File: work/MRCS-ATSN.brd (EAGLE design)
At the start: 159.8 x 68.8 mm, 63 parts, among them IC1 LM324N, IC2 LM324N, J1 RJ14, J2 RJ14, Q1 2N4401, Q2 2N4403, T1 TY-145P

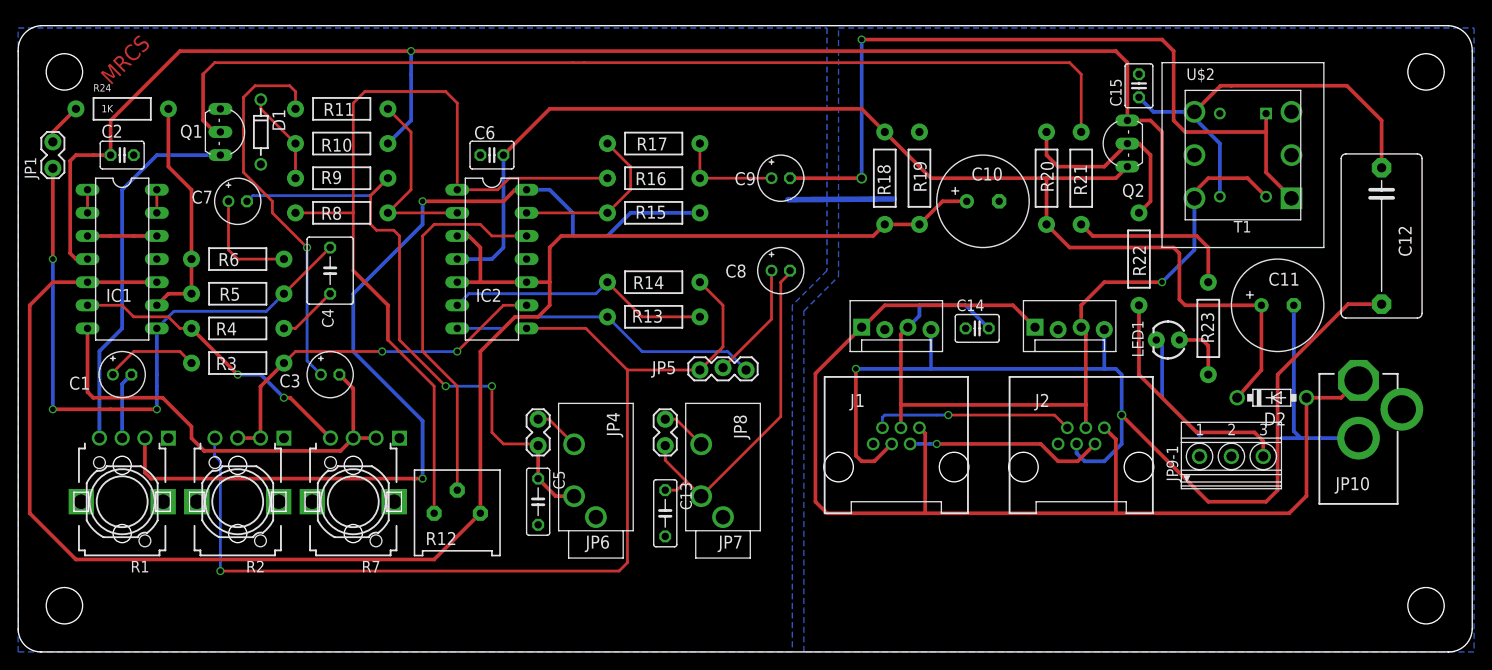
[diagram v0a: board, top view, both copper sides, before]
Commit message: clean up of messy import
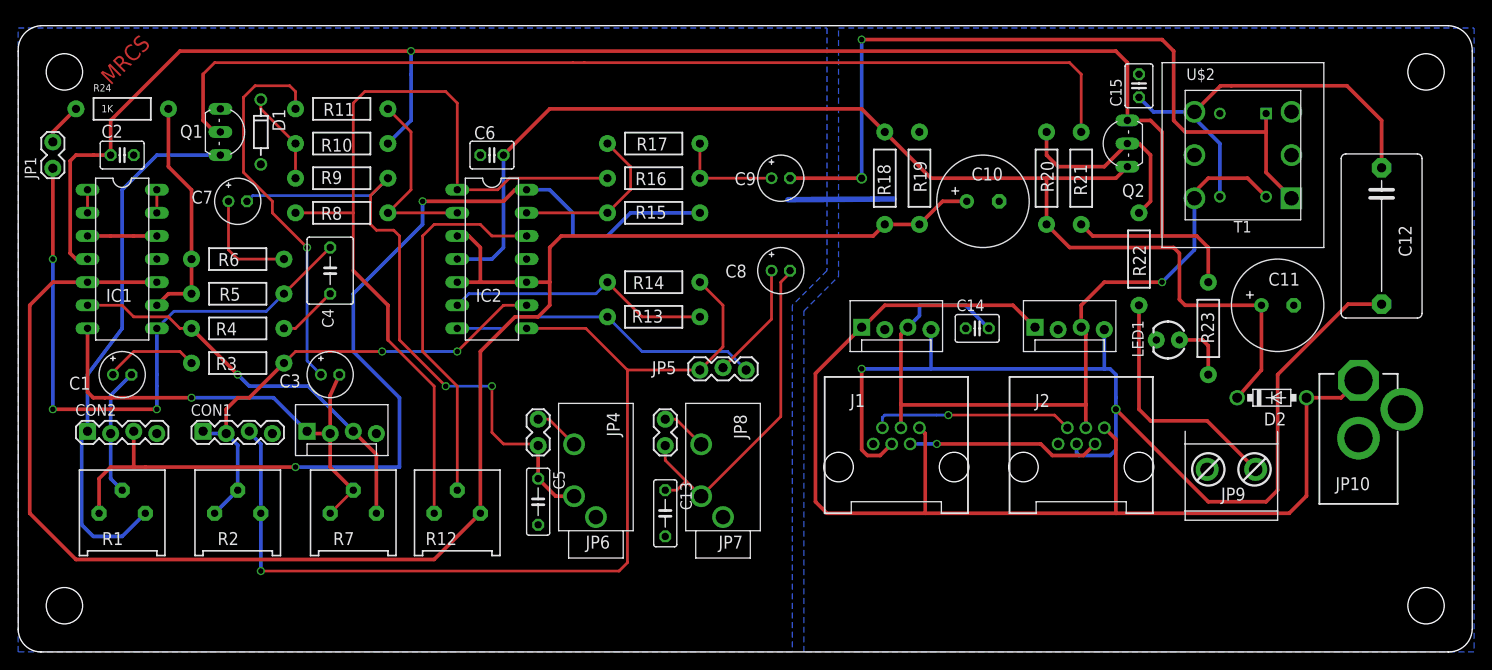
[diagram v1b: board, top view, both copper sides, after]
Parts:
- removed JP9-1: 1751251, con-phoenix-350:1751251
- added CON1: Audio, SPCoast 2017_04:1X04_LOCK
- added CON2: Break-In, SPCoast 2017_04:1X04_LOCK
- added JP9: (no value), SPCoast:MSTB2
- added SL3: (no value), SPCoast:MOLEX-1X4_LOCK
- C10, C11: device rcl:E3,5-10 -> rcl:E3.5-10
- POWER: device SPCoast:PWR_LABEL -> SPCoast:POWER_USAGE
- R1: value 10kA -> 10K; device SPCoast:R-POT-MRCS -> bourns_test:3386K
- R2: value 100kA -> 100K; device SPCoast:R-POT-MRCS -> bourns_test:3386K
- R7: value 500kA -> 500K; device SPCoast:R-POT-MRCS -> bourns_test:3386K
- moved R1 1.27 mm to (11.4, 15.2), turned to 0 degrees
- moved R2 1.27 mm to (24.1, 15.2), turned to 0 degrees
- moved R7 1.27 mm to (36.8, 15.2), turned to 0 degrees
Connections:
- removed net N$9: JP9-1.3, R22.P$1
- new net N$16: JP9.2, R22.P$1
- net GND: now also CON1.4, CON2.4, JP9.1, SL3.4; no longer JP9-1.1, JP9-1.2, R1.GND, R1.M1, R1.M2, R2.GND, R2.M1, R2.M2, R7.GND, R7.M1, R7.M2
- net N$13: now also SL3.1, SL3.2
- net N$20: now also CON1.1, CON1.2
- net N$38: now also SL3.3
- net N$40: now also CON1.3
- net RXGAIN: now also CON2.2
- net RXLEVEL: now also CON2.3
- net TXGND: now also CON2.1
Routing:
- net GND: track 47.5 -> 11.7 mm
- net N$16: track 0.00 -> 27.0 mm
- net N$9: track 26.0 -> 0.00 mm
- net TXGND: track 40.7 -> 59.3 mm
- net N$20: track 41.1 -> 53.5 mm
- net N$38: track 32.8 -> 45.0 mm, vias 2 -> 1
- net RXGAIN: track 7.39 -> 14.2 mm
- net RXLEVEL: track 107.0 -> 111.4 mm
- net N$40: track 113.9 -> 110.7 mm
- net N$13: track 50.3 -> 53.1 mm, vias 0 -> 1
- net RING: track 116.4 -> 113.7 mm
- net N$7: track 21.9 -> 21.4 mm
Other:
- board text added: "2017-08"
- board text added: "White soldermask / Black silkscreen"
- board text added: "rev 0.5"
- board text removed: "20170813"
- board text removed: "20181123"
- board text removed: "rev 0.6"
